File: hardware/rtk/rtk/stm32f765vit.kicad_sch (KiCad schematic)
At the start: 20 parts, among them J6 MEM2052-00-195-00-A_REVA, J7 Conn_01x04_Pin, U3 STM32F765VITx, U5 ESP32-S3-ZERO, U6 CORE1262-868M, U7 LSM6DSOX

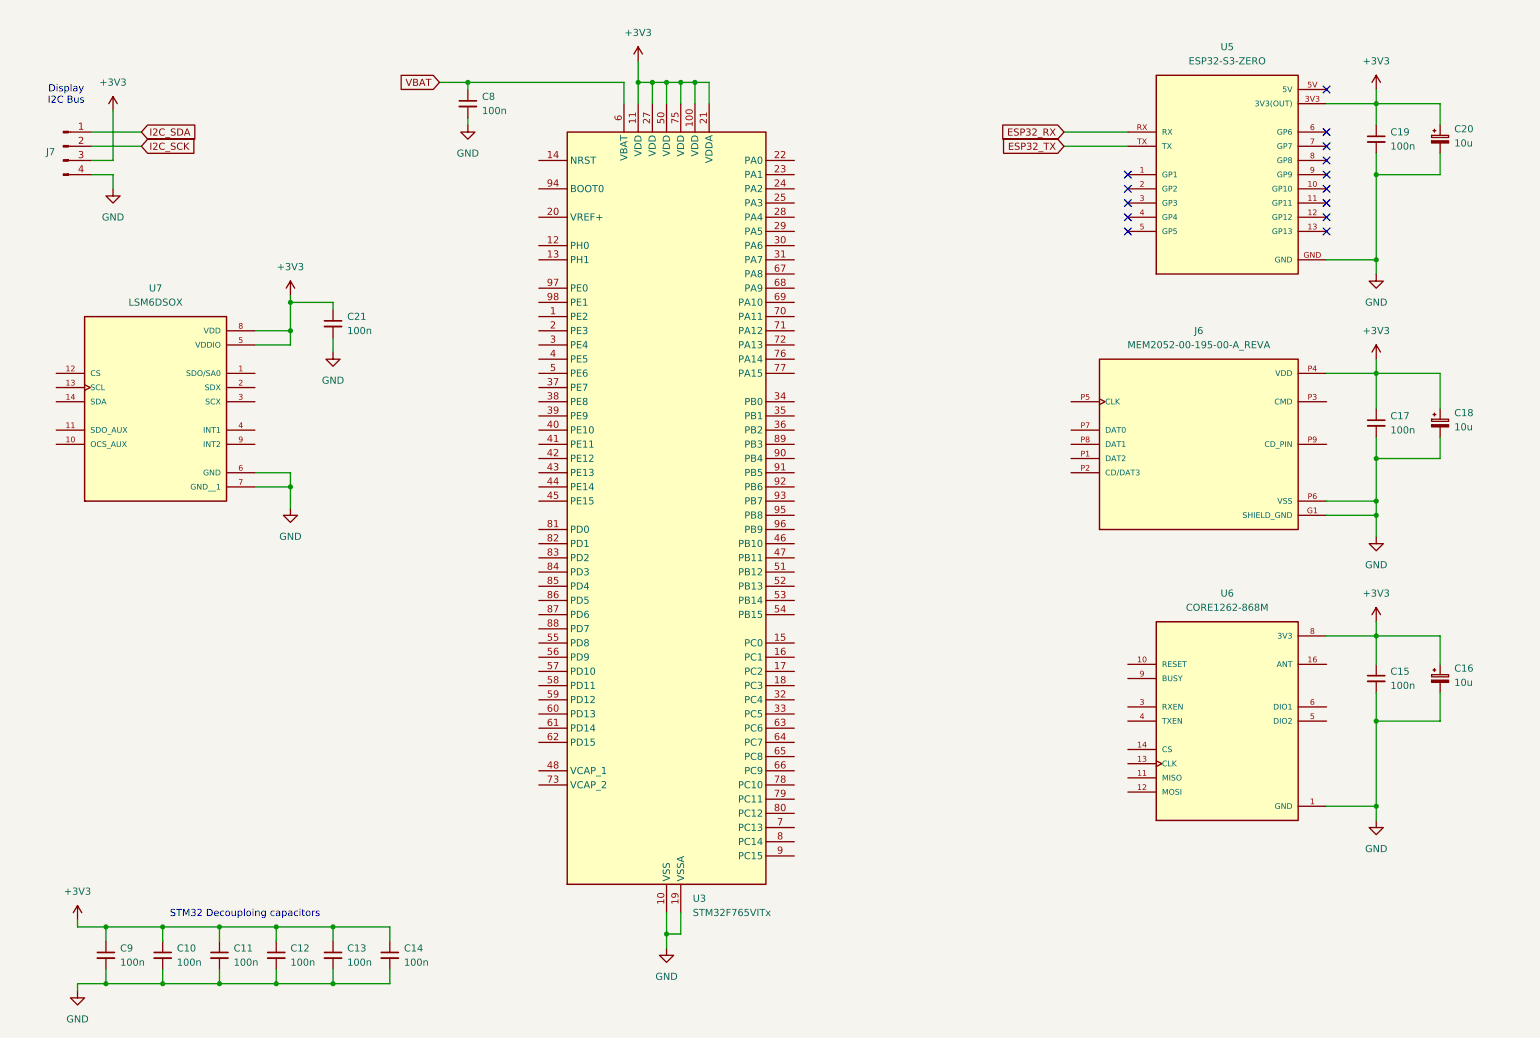
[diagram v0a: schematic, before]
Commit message: Hardware schematic progress: F765 pin assignments, USB HS, TCXO (#182)
- STM32F765VIT pin assignments via CubeMX (rtk-base.ioc updated)
- USB HS hierarchical sheet added (usb2hs.kicad_sch): USB3300 ULPI PHY,
  all 13 ULPI signals wired, reset GPIO, SOF test point
- ASTX-H11-16.000MHZ-T TCXO symbol + footprint added
- USB3300-EZK-TR symbol + footprint added
- USB3300-EZK-TR datasheet added to docs/datasheets/ + catalog updated
- PSU, STM32, ZED-F9P schematic sheets updated
- docs/reference/psu/README.md BQ24075 entry included

Co-Authored-By: Claude Sonnet 4.6 <noreply@anthropic.com>
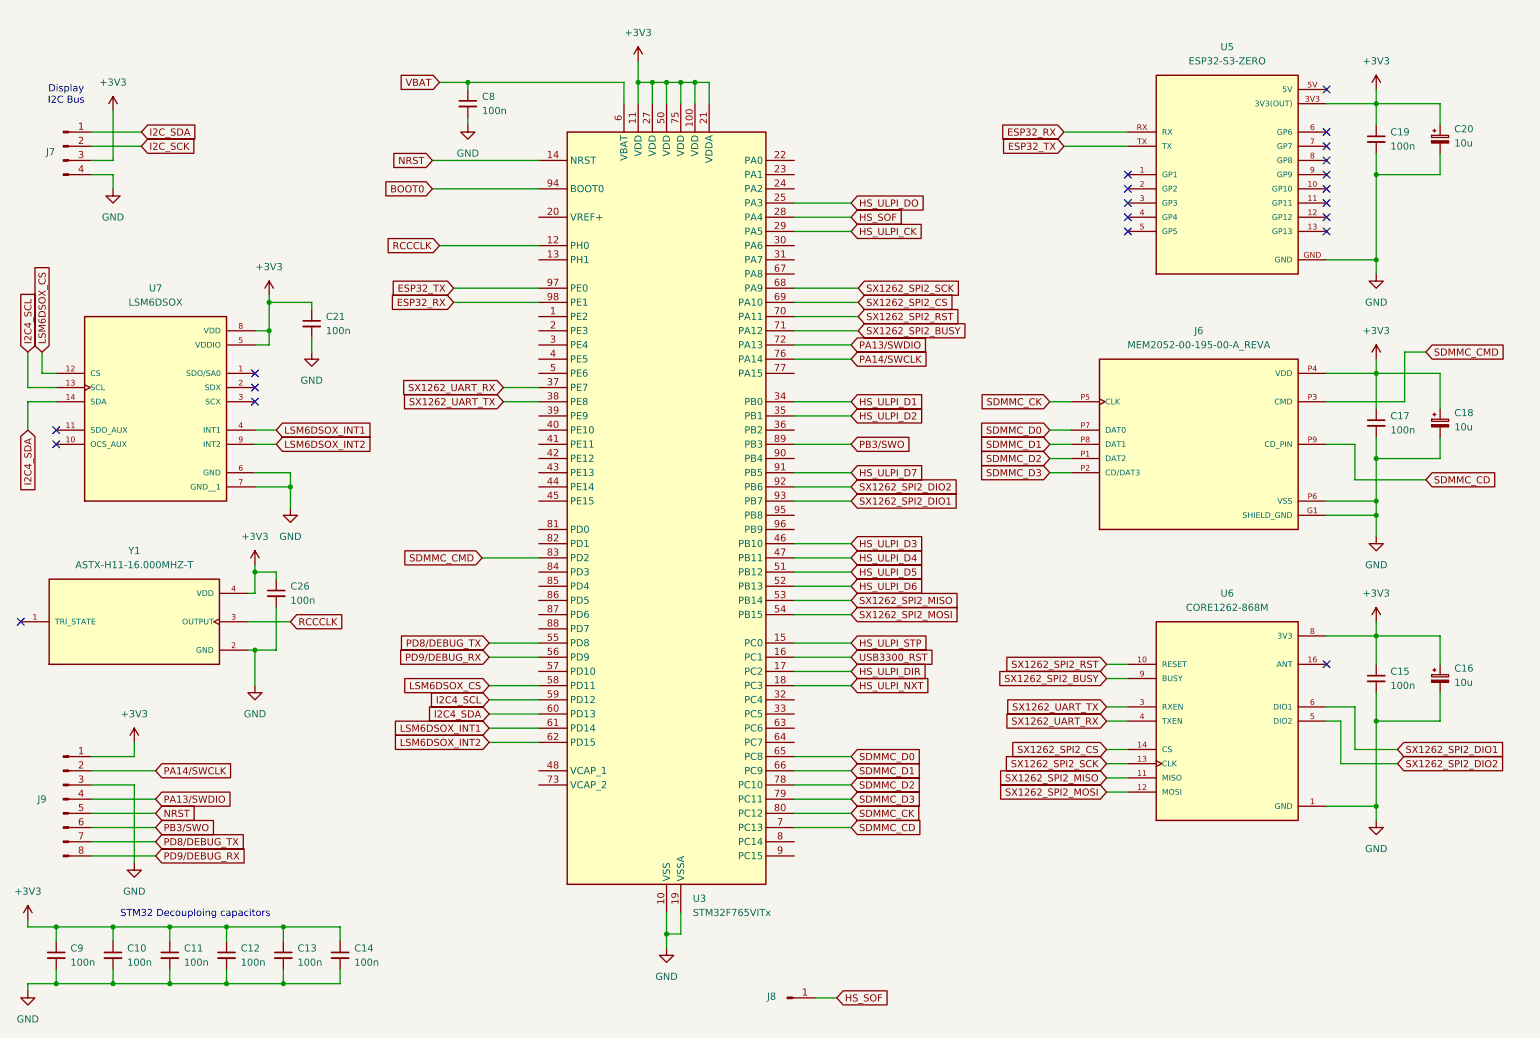
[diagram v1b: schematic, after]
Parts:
- added C26: 100n, Capacitor_SMD:C_0805_2012Metric_Pad1.18x1.45mm_HandSolder, symbol Device:C_Small
- added J8: Conn_01x01_Pin, Connector_PinHeader_2.54mm:PinHeader_1x01_P2.54mm_Vertical, symbol Connector:Conn_01x01_Pin
- added J9: Conn_01x08_Pin, Connector_PinHeader_2.54mm:PinHeader_1x08_P2.54mm_Vertical, symbol Connector:Conn_01x08_Pin
- added Y1: ASTX-H11-16.000MHZ-T, ASTX-H11-16.000MHZ-T:XTAL_ASTX-H11-16.000MHZ-T, symbol ASTX-H11-16.000MHZ-T:ASTX-H11-16.000MHZ-T
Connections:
- net +3V3: now also C26.1, J9.1 (Pin_1), Y1.4 (VDD)
- net ESP32_RX: now also U3.98 (PE1)
- net ESP32_TX: now also U3.97 (PE0)
- net GND: now also C26.2, J9.3 (Pin_3), Y1.2 (GND)
- net SDMMC_D2: now reaches J6.P1 (DAT2)
- net SDMMC_D2: now also U3.78 (PC10)
- net SDMMC_D3: now reaches J6.P2 (CD/DAT3)
- net SDMMC_D3: now also U3.79 (PC11)
- net SDMMC_CMD: now reaches J6.P3 (CMD)
- net SDMMC_CMD: now also U3.83 (PD2)
- net SDMMC_CK: now reaches J6.P5 (CLK)
- net SDMMC_CK: now also U3.80 (PC12)
- net SDMMC_D0: now reaches J6.P7 (DAT0)
- net SDMMC_D0: now also U3.65 (PC8)
- net SDMMC_D1: now reaches J6.P8 (DAT1)
- net SDMMC_D1: now also U3.66 (PC9)
- net SDMMC_CD: now reaches J6.P9 (CD_PIN)
- net SDMMC_CD: now also U3.7 (PC13)
- net LSM6DSOX_CS: now reaches U7.12 (CS)
- net LSM6DSOX_CS: now also U3.58 (PD11)
- net I2C4_SCL: now reaches U7.13 (SCL)
- net I2C4_SCL: now also U3.59 (PD12)
- net I2C4_SDA: now reaches U7.14 (SDA)
- net I2C4_SDA: now also U3.60 (PD13)
- net LSM6DSOX_INT1: now reaches U7.4 (INT1)
- net LSM6DSOX_INT1: now also U3.61 (PD14)
- net LSM6DSOX_INT2: now reaches U7.9 (INT2)
- net LSM6DSOX_INT2: now also U3.62 (PD15)
- net SX1262_SPI2_RST: now reaches U6.10 (RESET)
- net SX1262_SPI2_RST: now also U3.70 (PA11)
- net SX1262_SPI2_MISO: now reaches U6.11 (MISO)
- net SX1262_SPI2_MISO: now also U3.53 (PB14)
- net SX1262_SPI2_MOSI: now reaches U6.12 (MOSI)
- net SX1262_SPI2_MOSI: now also U3.54 (PB15)
- net SX1262_SPI2_SCK: now reaches U6.13 (CLK)
- net SX1262_SPI2_SCK: now also U3.68 (PA9)
- net SX1262_SPI2_CS: now reaches U6.14 (CS)
- net SX1262_SPI2_CS: now also U3.69 (PA10)
- net SX1262_UART_TX: now reaches U6.3 (RXEN)
- net SX1262_UART_TX: now also U3.38 (PE8)
- net SX1262_UART_RX: now reaches U6.4 (TXEN)
- net SX1262_UART_RX: now also U3.37 (PE7)
- net SX1262_SPI2_DIO2: now reaches U6.5 (DIO2)
- net SX1262_SPI2_DIO2: now also U3.92 (PB6)
- net SX1262_SPI2_DIO1: now reaches U6.6 (DIO1)
- net SX1262_SPI2_DIO1: now also U3.93 (PB7)
- net SX1262_SPI2_BUSY: now reaches U6.9 (BUSY)
- net SX1262_SPI2_BUSY: now also U3.71 (PA12)
- net RCCCLK: now reaches U3.12 (PH0)
- net RCCCLK: now also Y1.3 (OUTPUT)
- net NRST: now reaches U3.14 (NRST)
- net NRST: now also J9.5 (Pin_5)
- net HS_ULPI_STP: now reaches U3.15 (PC0)
- net USB3300_RST: now reaches U3.16 (PC1)
- net HS_ULPI_DIR: now reaches U3.17 (PC2)
- net HS_ULPI_NXT: now reaches U3.18 (PC3)
- net HS_ULPI_DO: now reaches U3.25 (PA3)
- net HS_SOF: now reaches U3.28 (PA4)
- net HS_SOF: now also J8.1 (Pin_1)
- net HS_ULPI_CK: now reaches U3.29 (PA5)
- net HS_ULPI_D1: now reaches U3.34 (PB0)
- net HS_ULPI_D2: now reaches U3.35 (PB1)
- net HS_ULPI_D3: now reaches U3.46 (PB10)
- net HS_ULPI_D4: now reaches U3.47 (PB11)
- net HS_ULPI_D5: now reaches U3.51 (PB12)
- net HS_ULPI_D6: now reaches U3.52 (PB13)
- net PD8/DEBUG_TX: now reaches U3.55 (PD8)
- net PD8/DEBUG_TX: now also J9.7 (Pin_7)
- net PD9/DEBUG_RX: now reaches U3.56 (PD9)
- net PD9/DEBUG_RX: now also J9.8 (Pin_8)
- net PA13/SWDIO: now reaches U3.72 (PA13)
- net PA13/SWDIO: now also J9.4 (Pin_4)
- net PA14/SWCLK: now reaches U3.76 (PA14)
- net PA14/SWCLK: now also J9.2 (Pin_2)
- net PB3/SWO: now reaches U3.89 (PB3)
- net PB3/SWO: now also J9.6 (Pin_6)
- net HS_ULPI_D7: now reaches U3.91 (PB5)
- net BOOT0: now reaches U3.94 (BOOT0)
- no-connect marks 14 -> 21
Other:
- moved on the sheet: C10, C11, C12, C13, C14, C21, C9

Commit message: Schematic progress: all sheets ~90% complete (#182)
- power.kicad_sch: PSU, BQ24075, LiPo connector, USB-C power path
- stm32f765vit.kicad_sch: F765VIT pin assignments, SPI2/I2C4/SDMMC1/UART7/8/USART3
- usb2hs.kicad_sch: USB3300 ULPI, 24MHz TCXO (ASTX-H11-24MHz), USB-C connector, diff pair nets USB_D+/USB_D-
- zed-f9p-05b.kicad_sch: ZED-F9P-05B connections
- rtk-base.ioc: DIO1 corrected to GPIO_Input, LSM6DSOX CS removed (I2C mode, CS tied high in schematic), DIO2 label typo fixed
- rtk.kicad_pcb/pro: project settings updated

Co-Authored-By: Claude Sonnet 4.6 <noreply@anthropic.com>
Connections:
- net I2C_SDA is gone; now on net I2C4_SDA: J7.1 (Pin_1)
- net +3V3: now also U7.12 (CS)
- net F9P_ANT_DETECT: now reaches U3.32 (PC4)
- net F9P_ANT_OFF: now reaches U3.33 (PC5)
- net F9P_ANT_SHORT: now reaches U3.36 (PB2)
- net F9P_TIMEP: now reaches U3.40 (PE10)
- net F9P_EXTINT: now reaches U3.41 (PE11)
- net F9P_SAFEBOOT_N: now reaches U3.42 (PE12)
- net F9P_RESET_N: now reaches U3.43 (PE13)
- net F9P_D_SEL: now reaches U3.44 (PE14)
- net F9P_TX_READY: now reaches U3.45 (PE15)
- net F9P_RX: now reaches U3.95 (PB8)
- net F9P_TX: now reaches U3.96 (PB9)
- net I2C_SCK renamed I2C4_SCK
- net LSM6DSOX_CS: no longer names the net of U3.58 (PD11)
- net LSM6DSOX_CS: no longer U7.12 (CS)

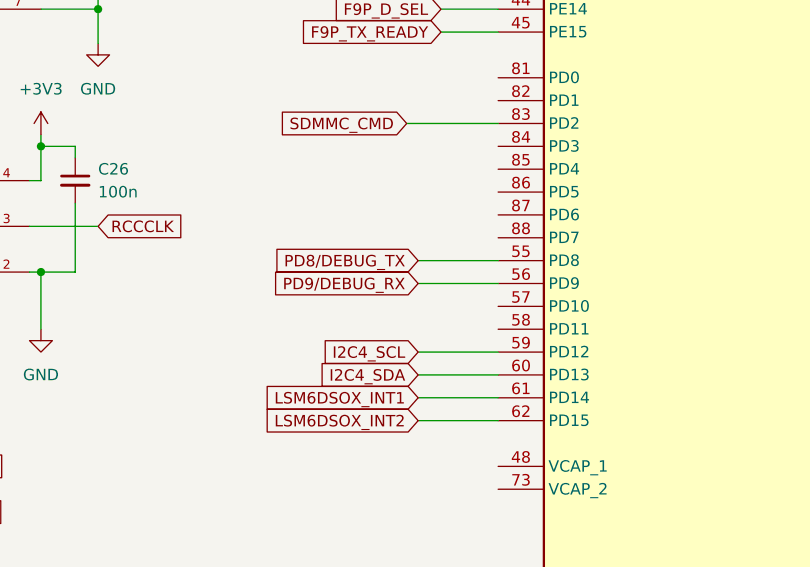
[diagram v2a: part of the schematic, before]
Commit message: Power sheet review fixes; SLVA553 inrush mitigation added (#182)
- power.kicad_sch: CC1/CC2 5.1k pull-downs on J1+J2, FB divider wiring
  fixed, TPS63020 inrush D1+C_SS per SLVA553, 1M NF bleed resistor
  across C_SS, TS NF 82k5 resistor added, nPGOOD/nCHG net labels added
- stm32f765vit.kicad_sch: nPGOOD→PD10, nCHG→PD11, SYSOFF→PD7 inputs added
- firmware/rtk-base/rtk-base.ioc: PD7/PD10/PD11 assigned
- docs/datasheets/slva553.pdf: TI SLVA553 app note (TPS6302x inrush)

Co-Authored-By: Claude Sonnet 4.6 <noreply@anthropic.com>
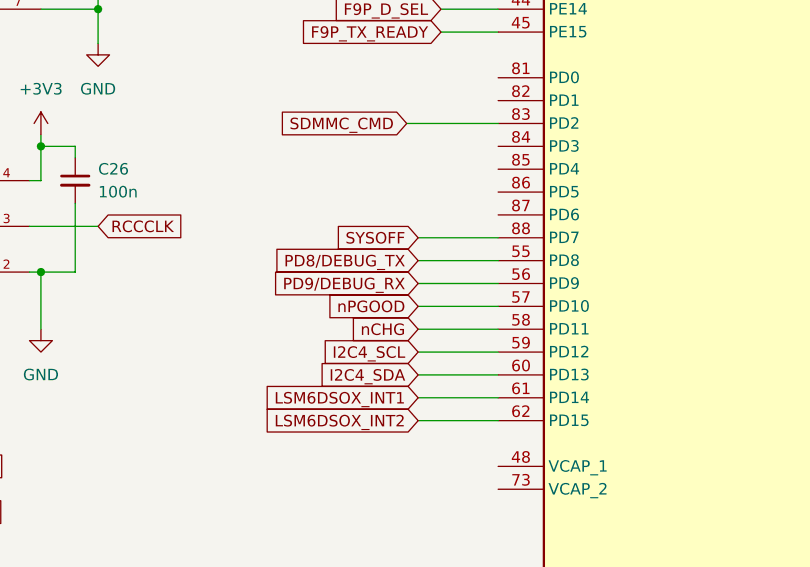
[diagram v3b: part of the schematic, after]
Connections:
- net nPGOOD: now reaches U3.57 (PD10)
- net nCHG: now reaches U3.58 (PD11)
- net SYSOFF: now reaches U3.88 (PD7)
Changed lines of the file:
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@@
+	(wire
+		(pts
+			(xy 99.06 132.08) (xy 107.95 132.08)
+		)
+		(stroke
+			(width 0)
+			(type default)
+		)
+	)
 	(wire
 		(pts
@@
 	(wire
 		(pts
+			(xy 99.06 134.62) (xy 107.95 134.62)
+		)
+		(stroke
+			(width 0)
+			(type default)
+		)
+	)
+	(wire
+		(pts
 			(xy 269.24 93.98) (xy 257.81 93.98)
 		)
@@
 	(wire
 		(pts
+			(xy 99.06 124.46) (xy 107.95 124.46)
+		)
+		(stroke
+			(width 0)
+			(type default)
+		)
+	)
+	(wire
+		(pts
 			(xy 153.67 134.62) (xy 163.83 134.62)
 		)
@@
 		)
 	)
+	(global_label "nCHG"
+		(shape input)
+		(at 99.06 134.62 180)
+		(fields_autoplaced yes)
+		(effects
+			(font
+				(size 1.27 1.27)
+			)
+			(justify right)
+		)
+		(property "Intersheetrefs" "${INTERSHEET_REFS}"
+			(at 91.0553 134.62 0)
+			(hide yes)
+			(show_name no)
+			(do_not_autoplace no)
+			(effects
+				(font
+					(size 1.27 1.27)
+				)
+				(justify right)
+			)
+		)
+	)
 	(global_label "SX1262_UART_TX"
 		(shape input)
@@
 			(hide yes)
 			(show_name no)
+			(do_not_autoplace no)
+			(effects
+				(font
+					(size 1.27 1.27)
+				)
+				(justify right)
+			)
+		)
+	)
+	(global_label "SYSOFF"
+		(shape input)
+		(at 99.06 124.46 180)
+		(fields_autoplaced yes)
+		(effects
+			(font
+				(size 1.27 1.27)
+			)
+			(justify right)
+		)
+		(property "Intersheetrefs" "${INTERSHEET_REFS}"
+			(at 89.0595 124.46 0)
+			(hide yes)
+			(show_name no)
+			(do_not_autoplace no)
+			(effects
+				(font
+					(size 1.27 1.27)
+				)
+				(justify right)
+			)
+		)
+	)
+	(global_label "nPGOOD"
+		(shape input)
+		(at 99.06 132.08 180)
+		(fields_autoplaced yes)
+		(effects
+			(font
+				(size 1.27 1.27)
+			)
+			(justify right)
+		)
+		(property "Intersheetrefs" "${INTERSHEET_REFS}"
+			(at 88.4548 132.08 0)
+			(hide yes)
+			(show_name no)
